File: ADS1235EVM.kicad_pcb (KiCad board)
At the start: 2 copper layers, 50 x 25 mm, 64 parts, among them J1 Conn_01x04_Pin, J2 Conn_01x11_Pin, U1 ADS1235QWRHMRQ1, U2 LM27762, U5 UCC27524DGN

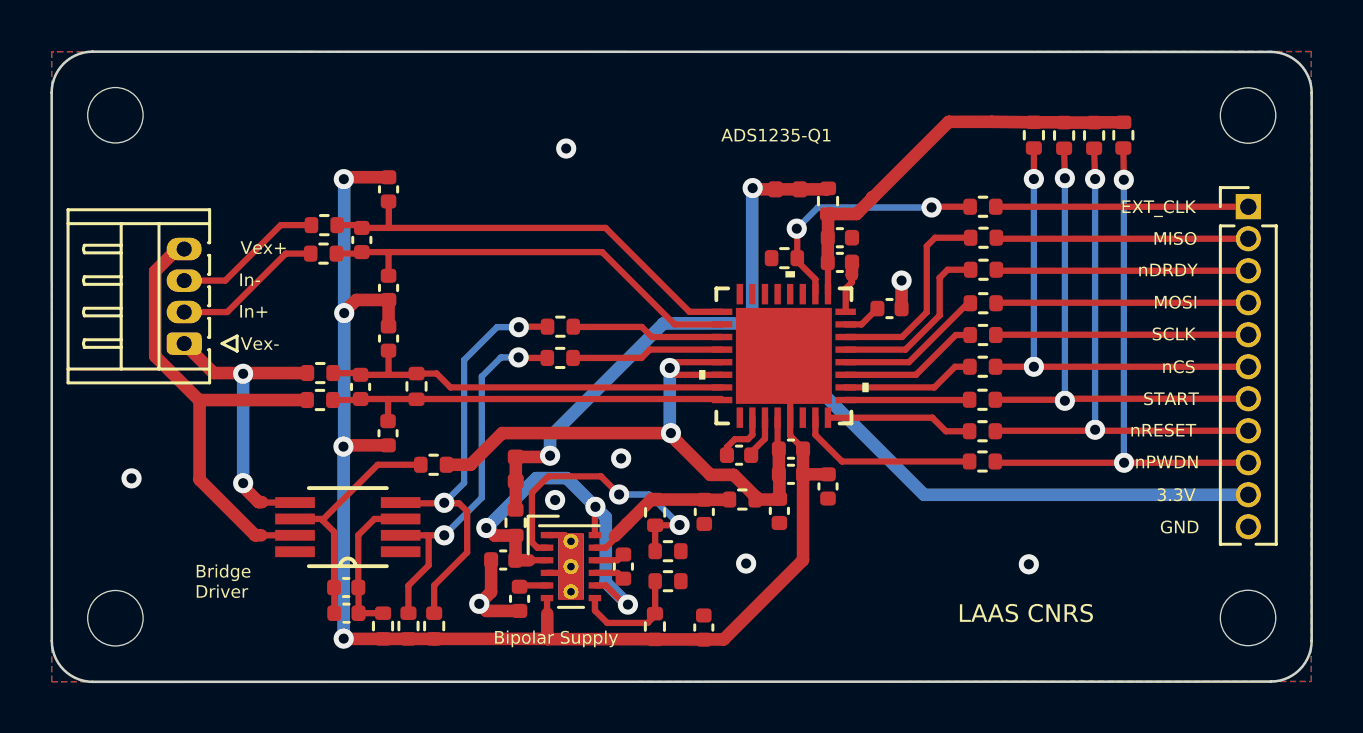
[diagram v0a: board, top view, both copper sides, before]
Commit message: PCB - Add of components name
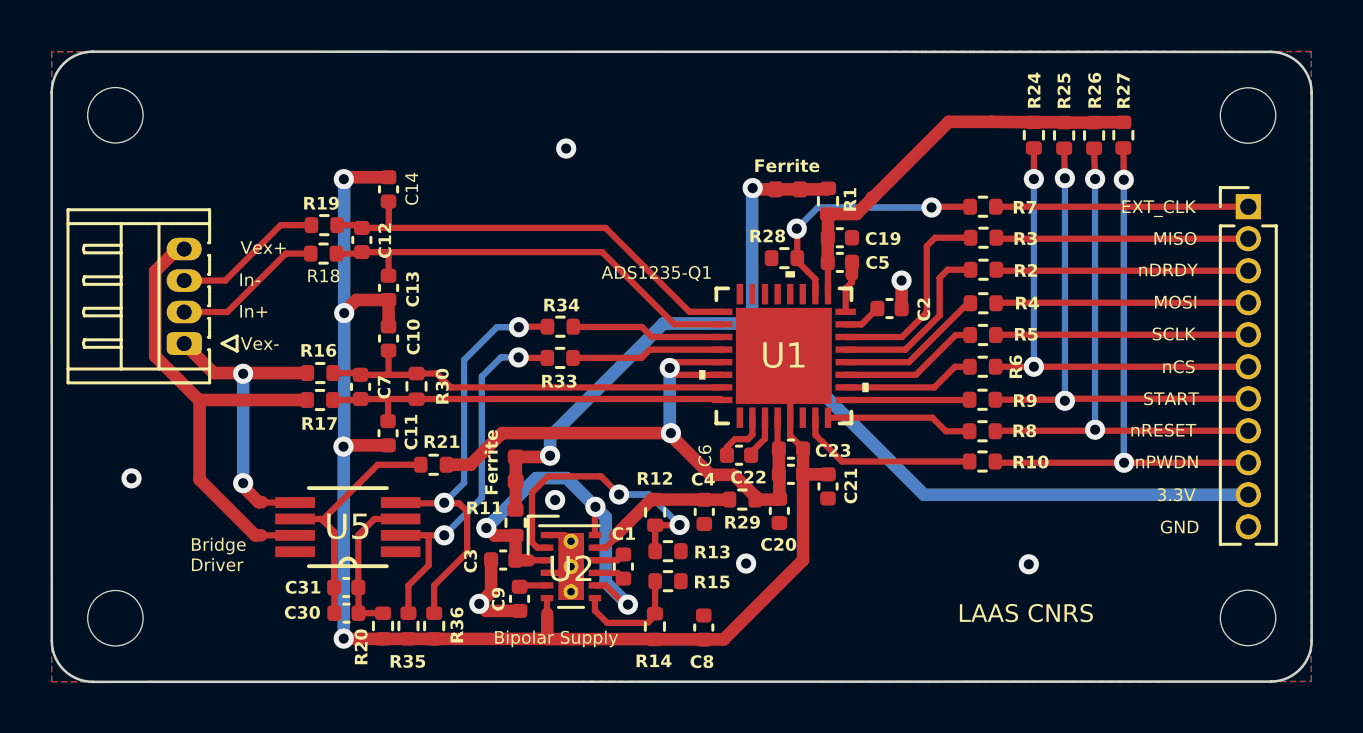
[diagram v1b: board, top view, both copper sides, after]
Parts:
- renumbered C to C23, REF** to Ferrite
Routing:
- net GND: vias 8 -> 7
